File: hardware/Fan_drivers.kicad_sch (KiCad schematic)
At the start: 28 parts, among them Q1 2SK3065, Q12 2SK3065, Q13 2SK3065, Q14 2SK3065, Q15 2SK3065, Q7 2SK3065, Q9 2SK3065

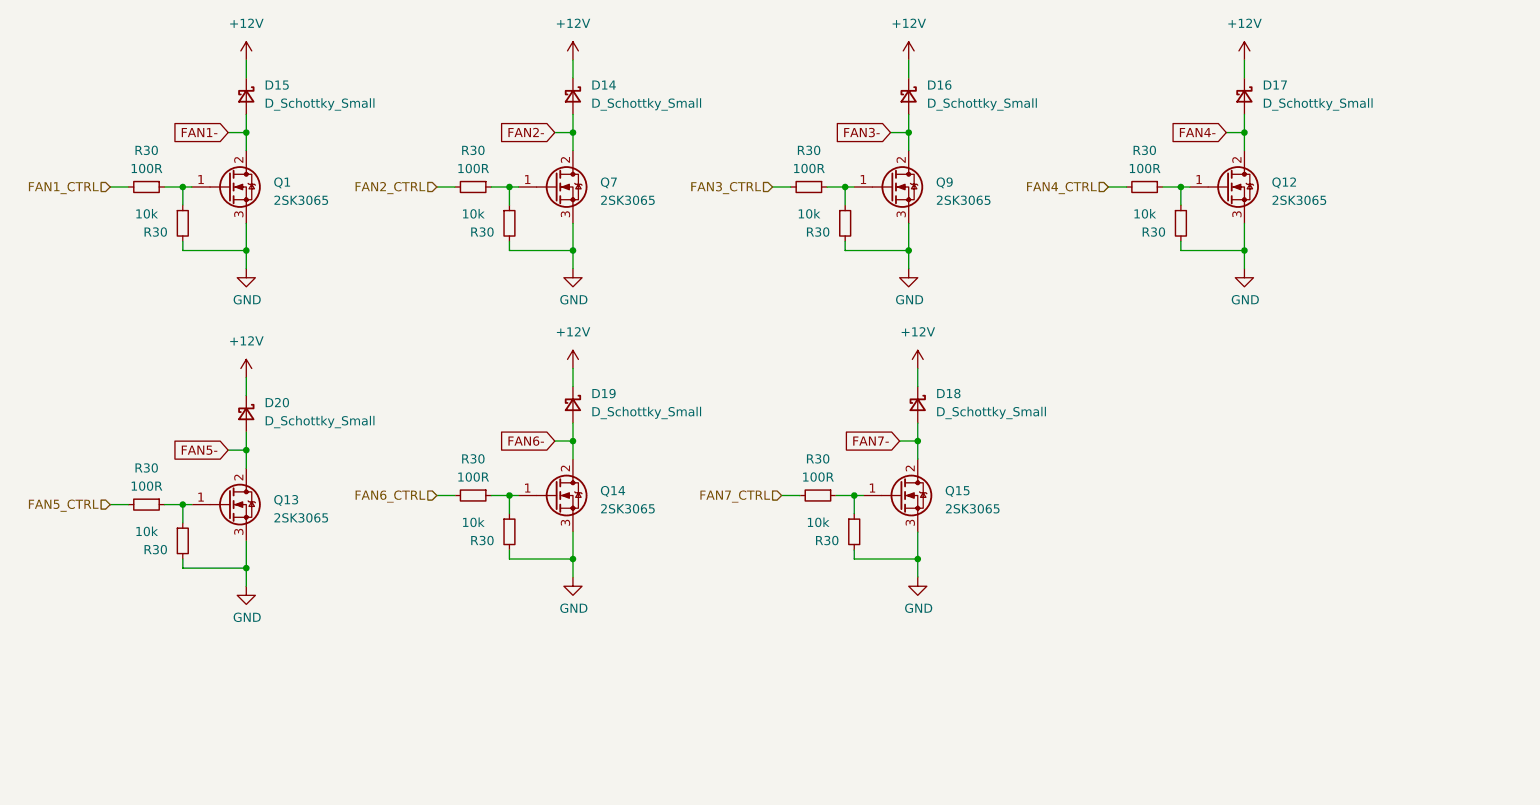
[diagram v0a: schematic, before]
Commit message: symbol update
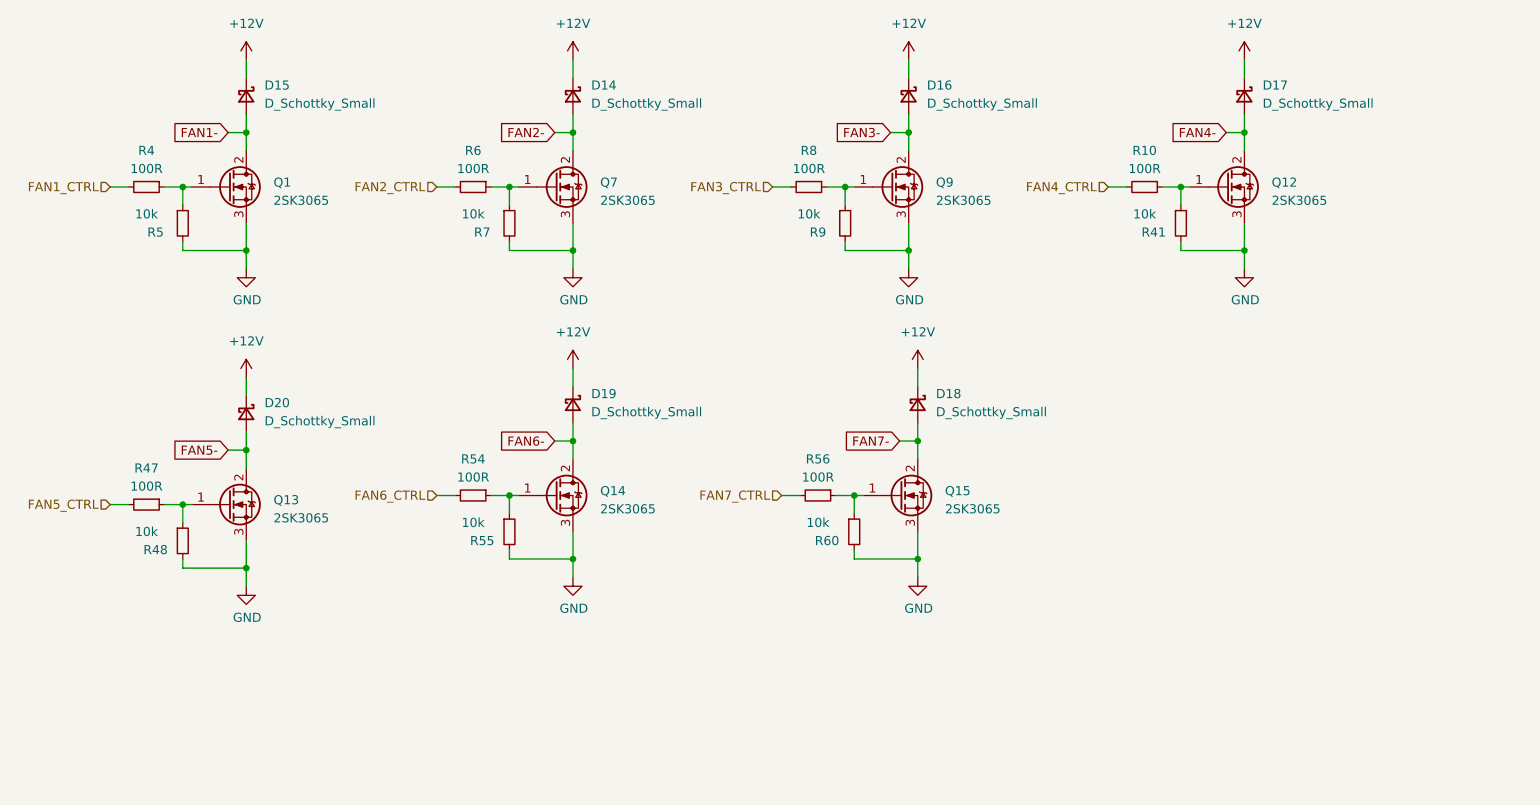
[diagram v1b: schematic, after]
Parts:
- renumbered R30 to R10, R30 to R4, R30 to R41, R30 to R47, R30 to R48, R30 to R5, R30 to R54, R30 to R55, R30 to R56, R30 to R6, R30 to R60, R30 to R7, R30 to R8, R30 to R9

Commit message: schematic clean up
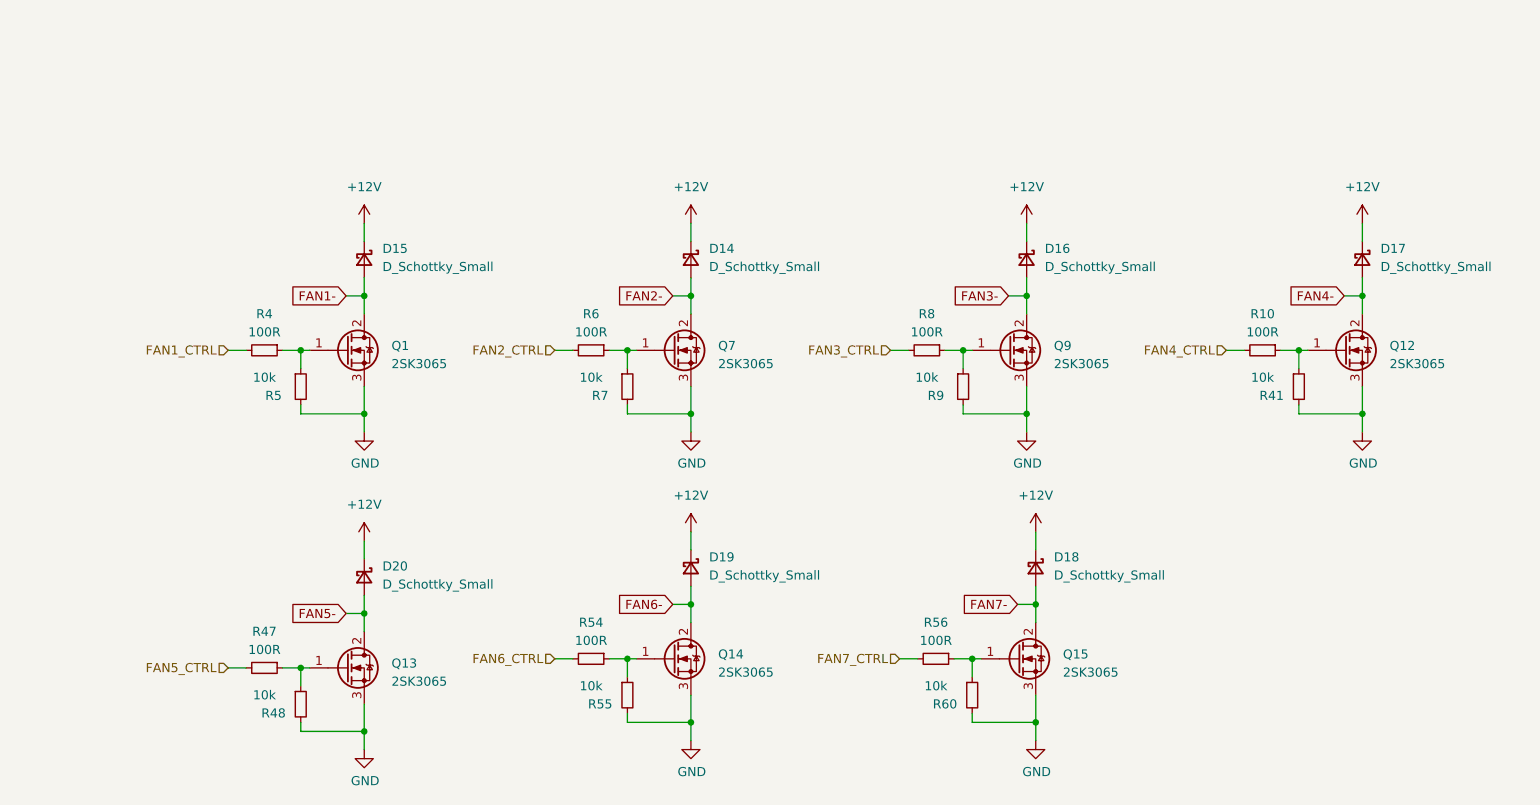
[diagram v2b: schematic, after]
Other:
- moved on the sheet: D14, D15, D16, D17, D18, D19, D20, Q1, Q12, Q13, Q14, Q15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

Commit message: relay new driving logic, some ltc communication changes
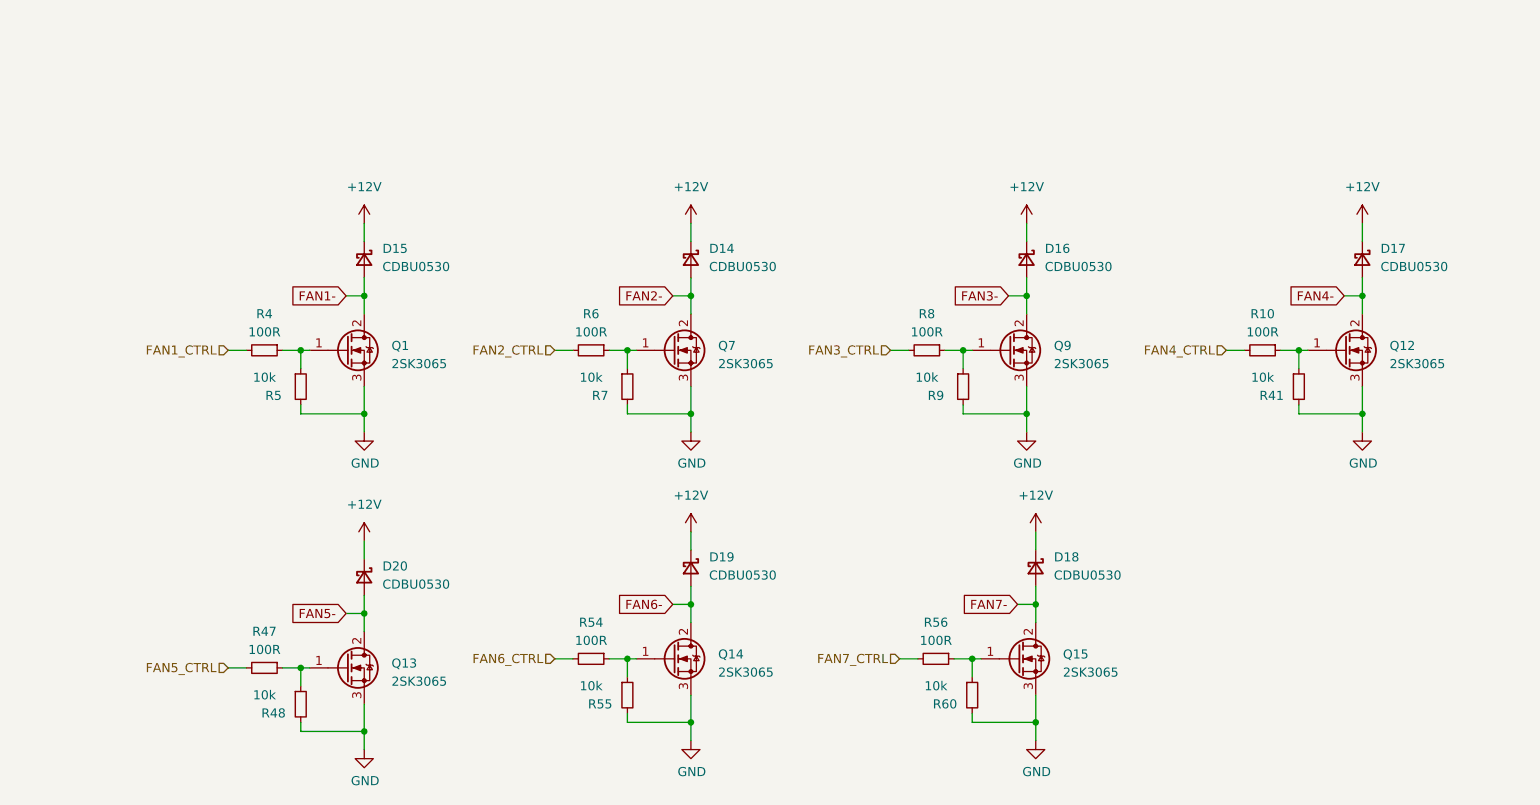
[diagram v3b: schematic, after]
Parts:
- D14, D15, D16, D17, D18, D19, D20: value D_Schottky_Small -> CDBU0530
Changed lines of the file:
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@@
 		(fields_autoplaced yes)
 		(property "Reference" "D18"
-			(at 189.23 111.506 90)
+			(at 189.23 111.5059 90)
 			(effects
 				(font
@@
 			)
 		)
-		(property "Value" "D_Schottky_Small"
-			(at 189.23 114.046 90)
+		(property "Value" "CDBU0530"
+			(at 189.23 114.0459 90)
 			(effects
 				(font
@@
 		(fields_autoplaced yes)
 		(property "Reference" "D20"
-			(at 95.25 112.776 90)
+			(at 95.25 112.7759 90)
 			(effects
 				(font
@@
 			)
 		)
-		(property "Value" "D_Schottky_Small"
-			(at 95.25 115.316 90)
+		(property "Value" "CDBU0530"
+			(at 95.25 115.3159 90)
 			(effects
 				(font
@@
 		(fields_autoplaced yes)
 		(property "Reference" "D14"
-			(at 140.97 68.326 90)
+			(at 140.97 68.3259 90)
 			(effects
 				(font
@@
 			)
 		)
-		(property "Value" "D_Schottky_Small"
-			(at 140.97 70.866 90)
+		(property "Value" "CDBU0530"
+			(at 140.97 70.8659 90)
 			(effects
 				(font
@@
 		(fields_autoplaced yes)
 		(property "Reference" "D17"
-			(at 234.95 68.326 90)
+			(at 234.95 68.3259 90)
 			(effects
 				(font
@@
 			)
 		)
-		(property "Value" "D_Schottky_Small"
-			(at 234.95 70.866 90)
+		(property "Value" "CDBU0530"
+			(at 234.95 70.8659 90)
 			(effects
 				(font
@@
 		(fields_autoplaced yes)
 		(property "Reference" "D19"
-			(at 140.97 111.506 90)
+			(at 140.97 111.5059 90)
 			(effects
 				(font
@@
 			)
 		)
-		(property "Value" "D_Schottky_Small"
-			(at 140.97 114.046 90)
+		(property "Value" "CDBU0530"
+			(at 140.97 114.0459 90)
 			(effects
 				(font
@@
 		(fields_autoplaced yes)
 		(property "Reference" "D16"
-			(at 187.96 68.326 90)
+			(at 187.96 68.3259 90)
 			(effects
 				(font
@@
 			)
 		)
-		(property "Value" "D_Schottky_Small"
-			(at 187.96 70.866 90)
+		(property "Value" "CDBU0530"
+			(at 187.96 70.8659 90)
 			(effects
 				(font
@@
 		(fields_autoplaced yes)
 		(property "Reference" "D15"
-			(at 95.25 68.326 90)
+			(at 95.25 68.3259 90)
 			(effects
 				(font
@@
 			)
 		)
-		(property "Value" "D_Schottky_Small"
-			(at 95.25 70.866 90)
-			(effects
-				(font
+		(property "Value" "CDBU0530"
+			(at 95.25 70.8659 90)
+			(effects
+				(font

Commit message: relay new driving logic, some ltc communication changes
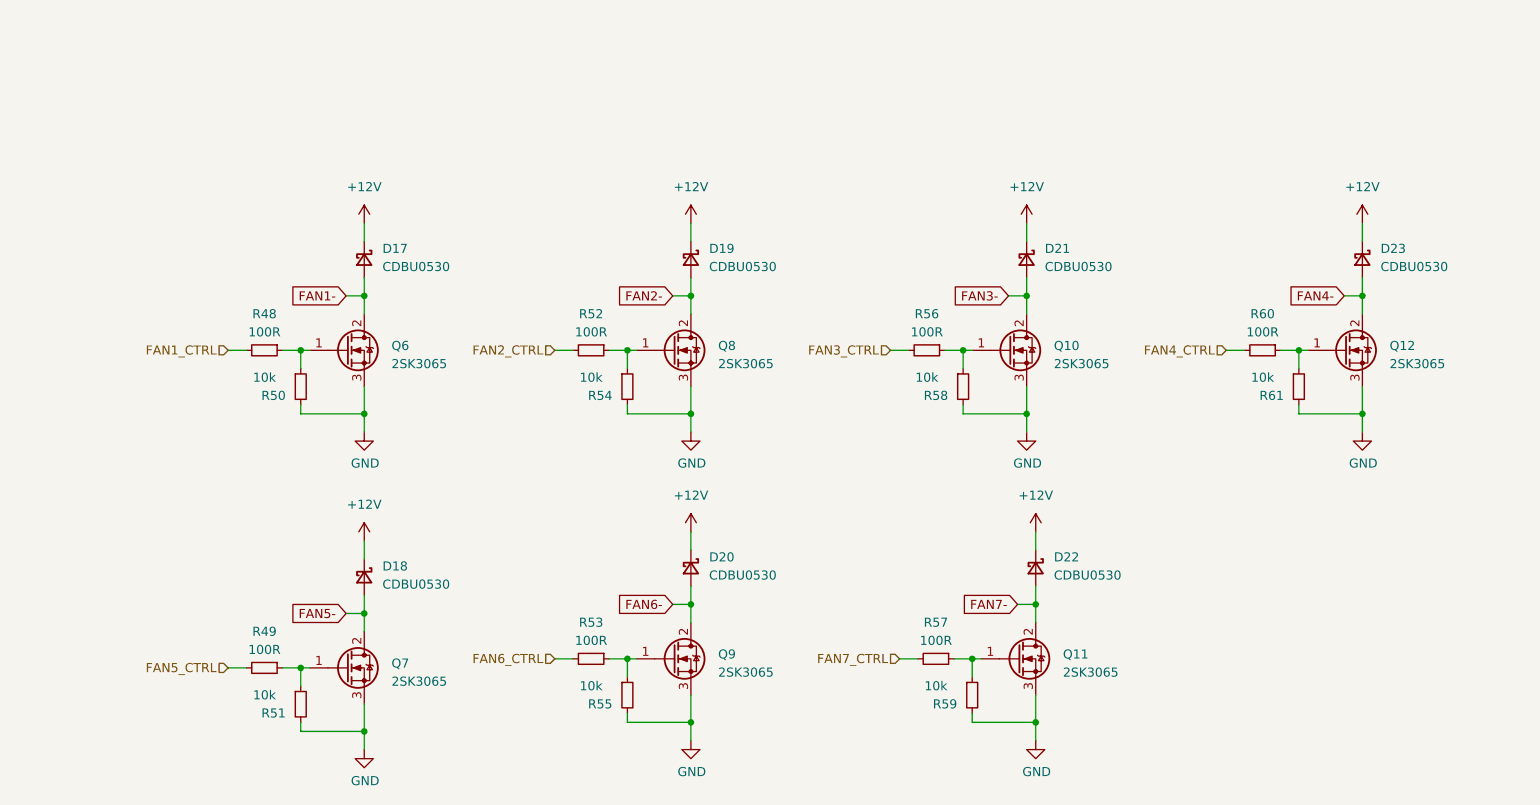
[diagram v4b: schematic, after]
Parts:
- renumbered D15 to D17, D20 to D18, D14 to D19, D19 to D20, D16 to D21, D18 to D22, D17 to D23, Q9 to Q10, Q15 to Q11, Q1 to Q6, Q13 to Q7, Q7 to Q8, Q14 to Q9, R4 to R48, R47 to R49, R5 to R50, R48 to R51, R6 to R52, R54 to R53, R7 to R54, R8 to R56, R56 to R57, R9 to R58, R60 to R59, R10 to R60, R41 to R61

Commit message: major schematic changes
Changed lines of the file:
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@@
 		)
 	)
-	(global_label "FAN5-"
-		(shape input)
-		(at 90.17 119.38 180)
-		(fields_autoplaced yes)
-		(effects
-			(font
-				(size 1.27 1.27)
-			)
-			(justify right)
-		)
-		(property "Intersheetrefs" "${INTERSHEET_REFS}"
-			(at 81.6288 119.38 0)
-			(effects
-				(font
-					(size 1.27 1.27)
-				)
-				(justify right)
-				(hide yes)
-			)
-		)
-	)
-	(global_label "FAN7-"
+	(hierarchical_label "FAN7-"
 		(shape input)
 		(at 184.15 118.11 180)
@@
 			(justify right)
 		)
-		(property "Intersheetrefs" "${INTERSHEET_REFS}"
-			(at 175.6088 118.11 0)
-			(effects
-				(font
-					(size 1.27 1.27)
-				)
-				(justify right)
-				(hide yes)
-			)
-		)
 	)
-	(global_label "FAN3-"
+	(hierarchical_label "FAN3-"
 		(shape input)
 		(at 182.88 74.93 180)
@@
 			(justify right)
 		)
-		(property "Intersheetrefs" "${INTERSHEET_REFS}"
-			(at 174.3388 74.93 0)
-			(effects
-				(font
-					(size 1.27 1.27)
-				)
-				(justify right)
-				(hide yes)
-			)
-		)
 	)
-	(global_label "FAN4-"
+	(hierarchical_label "FAN5_CTRL"
 		(shape input)
-		(at 229.87 74.93 180)
+		(at 73.66 127 180)
 		(fields_autoplaced yes)
 		(effects
@@
 			(justify right)
 		)
-		(property "Intersheetrefs" "${INTERSHEET_REFS}"
-			(at 221.3288 74.93 0)
-			(effects
-				(font
-					(size 1.27 1.27)
-				)
-				(justify right)
-				(hide yes)
-			)
-		)
 	)
-	(global_label "FAN1-"
+	(hierarchical_label "FAN5-"
 		(shape input)
-		(at 90.17 74.93 180)
-		(fields_autoplaced yes)
-		(effects
-			(font
-				(size 1.27 1.27)
-			)
-			(justify right)
-		)
-		(property "Intersheetrefs" "${INTERSHEET_REFS}"
-			(at 81.6288 74.93 0)
-			(effects
-				(font
-					(size 1.27 1.27)
-				)
-				(justify right)
-				(hide yes)
-			)
-		)
-	)
-	(global_label "FAN6-"
-		(shape input)
-		(at 135.89 118.11 180)
-		(fields_autoplaced yes)
-		(effects
-			(font
-				(size 1.27 1.27)
-			)
-			(justify right)
-		)
-		(property "Intersheetrefs" "${INTERSHEET_REFS}"
-			(at 127.3488 118.11 0)
-			(effects
-				(font
-					(size 1.27 1.27)
-				)
-				(justify right)
-				(hide yes)
-			)
-		)
-	)
-	(global_label "FAN2-"
-		(shape input)
-		(at 135.89 74.93 180)
-		(fields_autoplaced yes)
-		(effects
-			(font
-				(size 1.27 1.27)
-			)
-			(justify right)
-		)
-		(property "Intersheetrefs" "${INTERSHEET_REFS}"
-			(at 127.3488 74.93 0)
-			(effects
-				(font
-					(size 1.27 1.27)
-				)
-				(justify right)
-				(hide yes)
-			)
-		)
-	)
-	(hierarchical_label "FAN5_CTRL"
-		(shape input)
-		(at 73.66 127 180)
+		(at 90.17 119.38 180)
 		(fields_autoplaced yes)
 		(effects
@@
 		(fields_autoplaced yes)
 		(effects
+			(font
+				(size 1.27 1.27)
+			)
+			(justify right)
+		)
+	)
+	(hierarchical_label "FAN1-"
+		(shape input)
+		(at 90.17 74.93 180)
+		(fields_autoplaced yes)
+		(effects
+			(font
+				(size 1.27 1.27)
+			)
+			(justify right)
+		)
+	)
+	(hierarchical_label "FAN6-"
+		(shape input)
+		(at 135.89 118.11 180)
+		(fields_autoplaced yes)
+		(effects
+			(font
+				(size 1.27 1.27)
+			)
+			(justify right)
+		)
+	)
+	(hierarchical_label "FAN2-"
+		(shape input)
+		(at 135.89 74.93 180)
+		(fields_autoplaced yes)
+		(effects
+			(font
+				(size 1.27 1.27)
+			)
+			(justify right)
+		)
+	)
+	(hierarchical_label "FAN4-"
+		(shape input)
+		(at 229.87 74.93 180)
+		(fields_autoplaced yes)
+		(effects

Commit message: fixed some footprints; shorted pcb board to 60x100; re-designed the HV & current measuring as well as LTC communication, all are in one TS section;
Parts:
- D17, D18, D19, D20, D21, D22, D23: footprint Diode_SMD:D_0603_1608Metric -> Diode_SMD:D_SOD-123
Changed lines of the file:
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@@
 			)
 		)
-		(property "Footprint" "Diode_SMD:D_0603_1608Metric"
+		(property "Footprint" "Diode_SMD:D_SOD-123"
 			(at 186.69 113.03 90)
 			(effects
@@
 			)
 		)
-		(property "Footprint" "Diode_SMD:D_0603_1608Metric"
+		(property "Footprint" "Diode_SMD:D_SOD-123"
 			(at 92.71 114.3 90)
 			(effects
@@
 			)
 		)
-		(property "Footprint" "Diode_SMD:D_0603_1608Metric"
+		(property "Footprint" "Diode_SMD:D_SOD-123"
 			(at 138.43 69.85 90)
 			(effects
@@
 			)
 		)
-		(property "Footprint" "Diode_SMD:D_0603_1608Metric"
+		(property "Footprint" "Diode_SMD:D_SOD-123"
 			(at 232.41 69.85 90)
 			(effects
@@
 			)
 		)
-		(property "Footprint" "Diode_SMD:D_0603_1608Metric"
+		(property "Footprint" "Diode_SMD:D_SOD-123"
 			(at 138.43 113.03 90)
 			(effects
@@
 			)
 		)
-		(property "Footprint" "Diode_SMD:D_0603_1608Metric"
+		(property "Footprint" "Diode_SMD:D_SOD-123"
 			(at 185.42 69.85 90)
 			(effects
@@
 			)
 		)
-		(property "Footprint" "Diode_SMD:D_0603_1608Metric"
+		(property "Footprint" "Diode_SMD:D_SOD-123"
 			(at 92.71 69.85 90)
 			(effects

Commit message: new beginings tbc
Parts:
- removed R48, R49, R52, R53, R56, R57, R60: 100R, Resistor_SMD:R_0603_1608Metric, symbol Device:R_Small
- removed R50, R51, R54, R55, R58, R59, R61: 10k, Resistor_SMD:R_0603_1608Metric, symbol Device:R_Small
- added RN1, RN9: 100, Resistor_SMD:R_Array_Convex_4x0603, symbol Device:R_Pack04_Split
- added RN10, RN8: 10k, Resistor_SMD:R_Array_Convex_4x0603, symbol Device:R_Pack04_Split
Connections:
- net FAN1_CTRL: now also RN1.8 (R1.2)
- net FAN2_CTRL: now also RN1.6 (R3.2)
- net FAN3_CTRL: now also RN9.8 (R1.2)
- net FAN4_CTRL: now also RN9.6 (R3.2)
- net FAN5_CTRL: now also RN1.7 (R2.2)
- net FAN6_CTRL: now also RN1.5 (R4.2)
- net FAN7_CTRL: now also RN9.7 (R2.2)
- net GND: now also RN10.1 (R1.1), RN10.2 (R2.1), RN10.3 (R3.1), RN8.1 (R1.1), RN8.2 (R2.1), RN8.3 (R3.1), RN8.4 (R4.1)
- net at Q12.1 (G): now also RN10.6 (R3.2), RN9.3 (R3.1)
- net at Q8.1 (G): now also RN1.3 (R3.1), RN8.6 (R3.2)
- net at Q10.1 (G): now also RN10.8 (R1.2), RN9.1 (R1.1)
- net at Q11.1 (G): now also RN10.7 (R2.2), RN9.2 (R2.1)
- net at Q9.1 (G): now also RN1.4 (R4.1), RN8.5 (R4.2)
- net at Q7.1 (G): now also RN1.2 (R2.1), RN8.7 (R2.2)
- net at Q6.1 (G): now also RN1.1 (R1.1), RN8.8 (R1.2)
- no-connect marks 0 -> 4
